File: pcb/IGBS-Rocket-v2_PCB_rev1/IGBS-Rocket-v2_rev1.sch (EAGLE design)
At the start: 220 parts, among them IC1 NCV21872DR2G, IC2 NCV21872DR2G, IC3 NCV21872DR2G, Q1 BC817, Q2 ENC-03, Q3 BSS316N-H6327, U1 STM32H750VBT6, U2 LM317BD2TG, U5 MICROSD, U6 ESP-12E/F, U8 LP324DRG4, U9 MCP6V51T-E/MS, Y1 24MHz

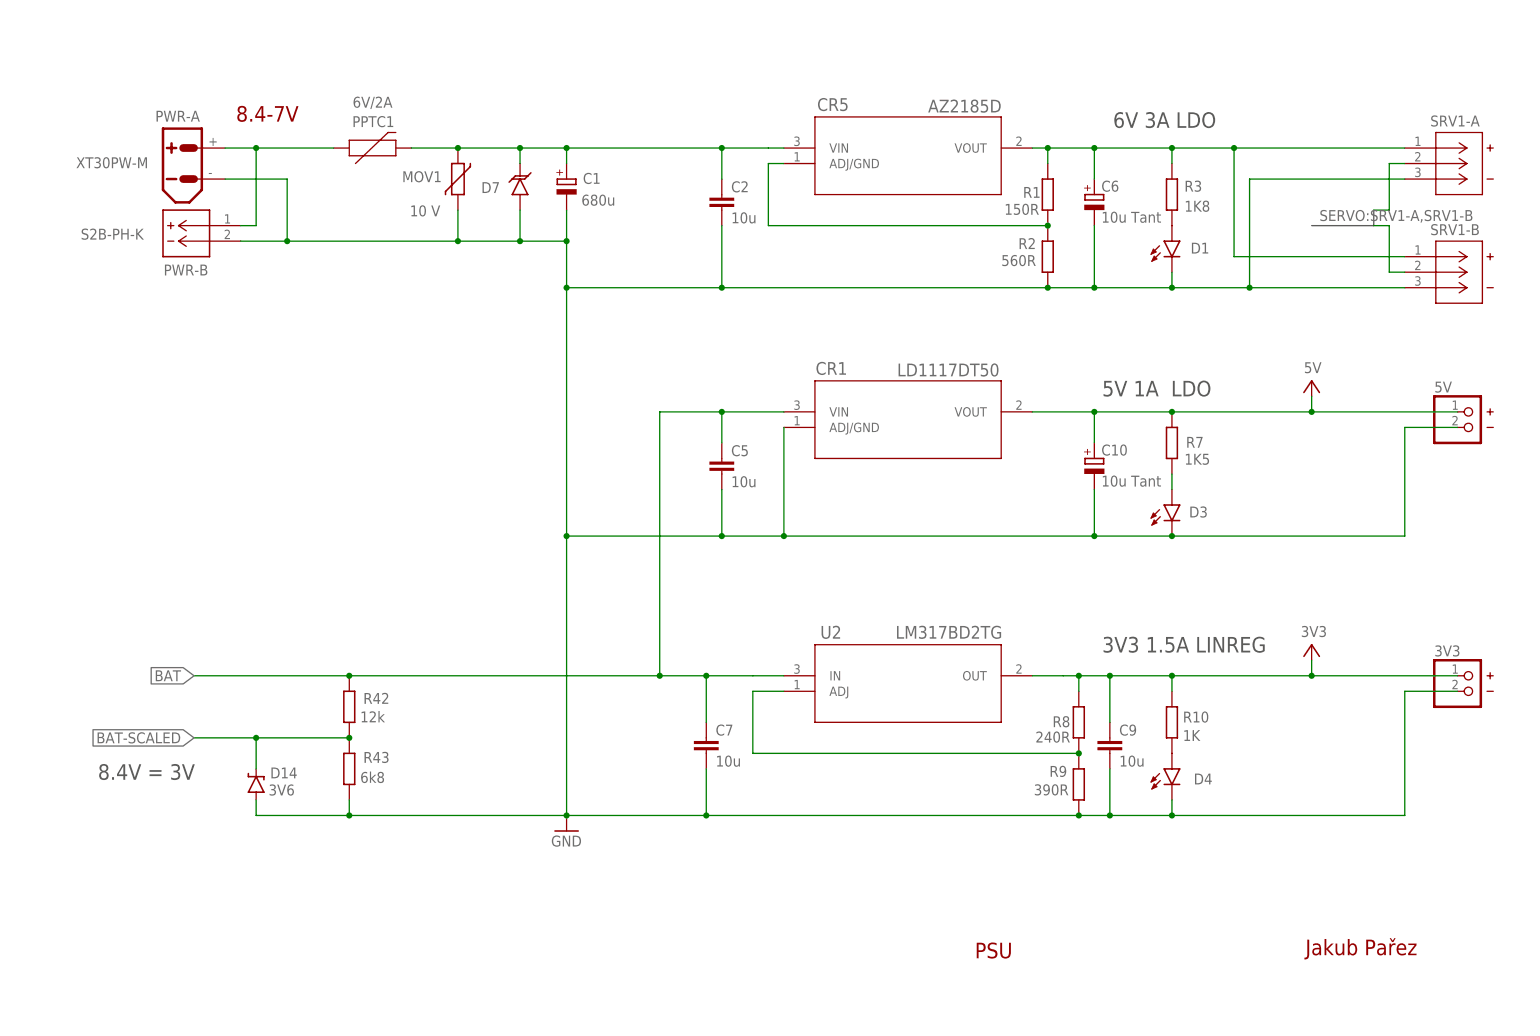
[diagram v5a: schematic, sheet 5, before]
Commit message: * PCB: 12V regulator added, P-FET HSS is now last missing part
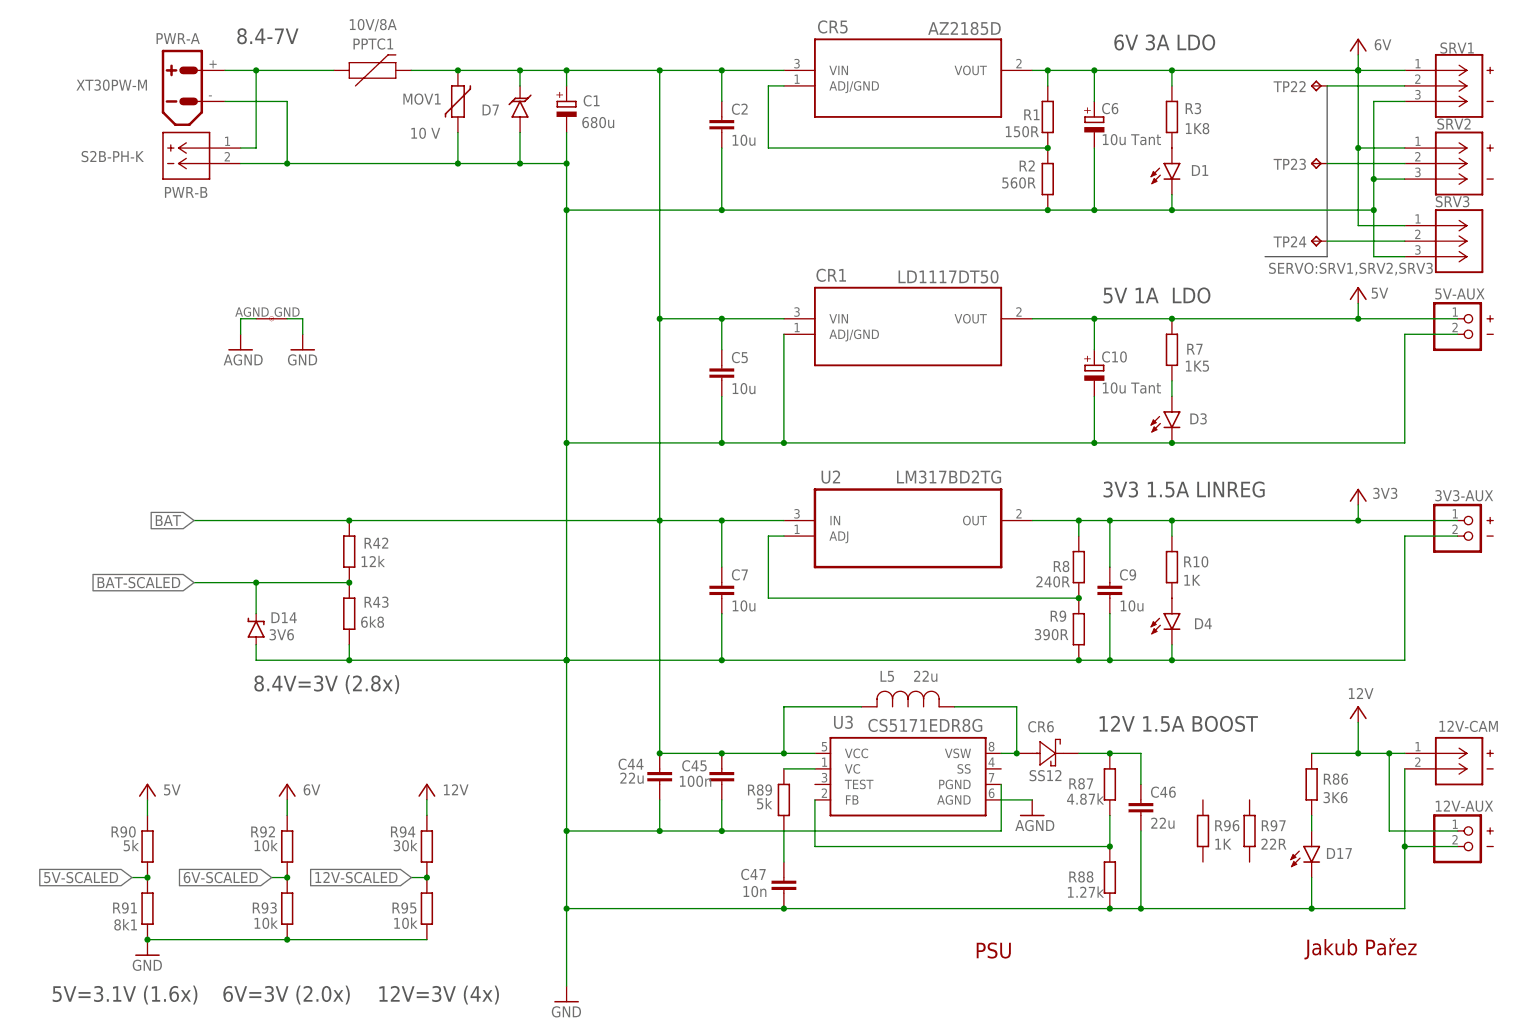
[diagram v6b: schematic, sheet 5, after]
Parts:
- removed 3V3, 5V: (no value), pinhead2:PINHD-1X2
- removed SRV1-B: S3B-XH-A(LF)(SN)CONN_S3B-XH-A(LF)(SN)_JST, jst-XH2:S3B-XH-A(LF)(SN)CONN_S3B-XH-A(LF)(SN)_JST
- added 12V-AUX, 3V3-AUX, 5V-AUX: (no value), pinhead2:PINHD-1X2
- added 12V-CAM: S2B-XH-A(LF)(SN)CONN_S2B-XH-A_JST, jst-XH2:S2B-XH-A(LF)(SN)CONN_S2B-XH-A_JST
- added C44, C46: 22u, SparkFun-Capacitors:10UF10V10%(0805)
- added C45: 100n, rcl2:C-EUC0805K
- added C47: 10n, rcl2:C-EUC0805K
- added CR6: SS12, diode2:SS12-E3/5ATDIODE_DO214AC
- added D17: GREEN, leds:LED-GREEN1206
- added L5: 22u, rcl2:744373240047IND_74437_WRE
- added R86: 3K6, rcl2:R-EU_R0603
- added R87: 4.87k, rcl2:R-EU_R0603
- added R88: 1.27k, rcl2:R-EU_R0603
- added R89, R90: 5k, rcl2:R-EU_R0603
- added R91: 8k1, rcl2:R-EU_R0603
- added R92, R93, R95: 10k, rcl2:R-EU_R0603
- added R94: 30k, rcl2:R-EU_R0603
- added R96: 1K, rcl2:R-EU_R0603
- added R97: 22R, rcl2:R-EU_R0603
- added SRV1: S3B-XH-A, jst-XH2:S3B-XH-A(LF)(SN)CONN_S3B-XH-A(LF)(SN)_JST
- added SRV3: S3B-XH-A(LF)(SN)CONN_S3B-XH-A(LF)(SN)_JST, jst-XH2:S3B-XH-A(LF)(SN)CONN_S3B-XH-A(LF)(SN)_JST
- added TP22, TP23, TP24: TPB1,27, testpad2:TPB1,27
- added U$1: SHORT, testpad2:SHORT
- added U3: CS5171EDR8G, dc-dc:CS5171EDR8GSOIC8_ONS
- GND-AUX: device pinhead2:PINHD-1X4 -> pinhead2:PINHD-1X2
- PPTC1: value 6V/2A -> 10V/8A
- SRV2: value S3B-XH-A -> S3B-XH-A(LF)(SN)CONN_S3B-XH-A(LF)(SN)_JST
- renumbered SRV1-A to SRV2
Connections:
- removed net 6V-1: C6.+, CR5.VOUT, R1.2, R3.2, SRV1-B.1, SRV2.1
- removed net SRV1-A: SRV2.2, U1A.PA0-WKUP
- removed net SRV1-B: SRV1-B.2, U1A.PA1
- new net 12V: 12V-AUX.1, 12V-CAM.1, R86.2, R94.2
- new net 12V-SCALED: R94.1, R95.2
- new net 5V-SCALED: R90.1, R91.2
- new net 6V: C6.+, CR5.VOUT, R1.2, R3.2, R92.2, SRV1.1, SRV2.1, SRV3.1
- new net 6V-SCALED: R92.1, R93.2
- new net AGND: C20.1, C25.1, C27.2, C29.1, C3.1, C30.1, C34.1, C35.1, C37.1, C38.1, C39.1, C40.1, C41.1, C42.1, C43.1, C8.1, CR2.2, CR2.3, CR3.2, CR3.3, CR4.2, CR4.3, D15.A, IC1P.V-, IC2P.V-, IC3P.V-, Q2.GND, R4.3, R6.2, R62.2, R68.3, R70.2, R71.2, R77.3, R79.2, R80.2, U$1.1, U1C.VSSA, U3.AGND, U8P.GND, U9P.GND
- new net N$27: CR6.2, L5.1, U3.VSW
- new net N$59: D17.A, R86.1
- new net N$67: C46.1, CR6.1, R87.2
- new net N$70: C47.2, R89.1
- new net N$71: R89.2, U3.VC
- new net SRV1: SRV1.2, TP22.TP, U1A.PA0-WKUP
- new net SRV2: SRV2.2, TP23.TP, U1A.PA1
- new net SRV3: SRV3.2, TP24.TP, U1A.PD14
- net 3V3: now also 3V3-AUX.1; no longer 3V3.1
- net 5V: now also 5V-AUX.1, R90.2; no longer 5V.1
- net BAT: now also C1.+, C2.1, C44.1, C45.2, CR5.VIN, D7.C, L5.2, MOV1.1, PPTC1.2, U3.VCC
- net GND: now also 12V-AUX.2, 12V-CAM.2, 3V3-AUX.2, 5V-AUX.2, C44.2, C45.1, C46.2, C47.1, D17.C, R88.1, R91.1, R93.1, R95.1, SRV1.3, SRV3.3, U$1.2, U3.PGND; no longer 3V3.2, 5V.2, C20.1, C25.1, C27.2, C29.1, C3.1, C30.1, C34.1, C35.1, C37.1, C38.1, C39.1, C40.1, C41.1, C42.1, C43.1, C8.1, CR2.2, CR2.3, CR3.2, CR3.3, CR4.2, CR4.3, D15.A, GND-AUX.3, GND-AUX.4, IC1P.V-, IC2P.V-, IC3P.V-, Q2.GND, R4.3, R6.2, R62.2, R68.3, R70.2, R71.2, R77.3, R79.2, R80.2, SRV1-B.3, U1C.VSSA, U8P.GND, U9P.GND
- net N$18: now also R87.1, R88.2, U3.FB; no longer C1.+, C2.1, CR5.VIN, D7.C, MOV1.1, PPTC1.2
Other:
- note added: "12V 1.5A BOOST"
- note added: "12V=3V (4x)"
- note added: "5V=3.1V (1.6x)"
- note added: "6V=3V (2.0x)"
- note added: "8.4V=3V (2.8x)"
- note added: "GAIN = 48 + (0 - 24.5) VOLT = 0 - 3.6V"
- note removed: "8.4V = 3V"
- moved on the sheet: C1, C10, C2, C5, C6, C7, C9, CR1, CR5, D1, D14, D3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

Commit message: + PCB schematics is DONE (added 12V BOOST + 3 servos)
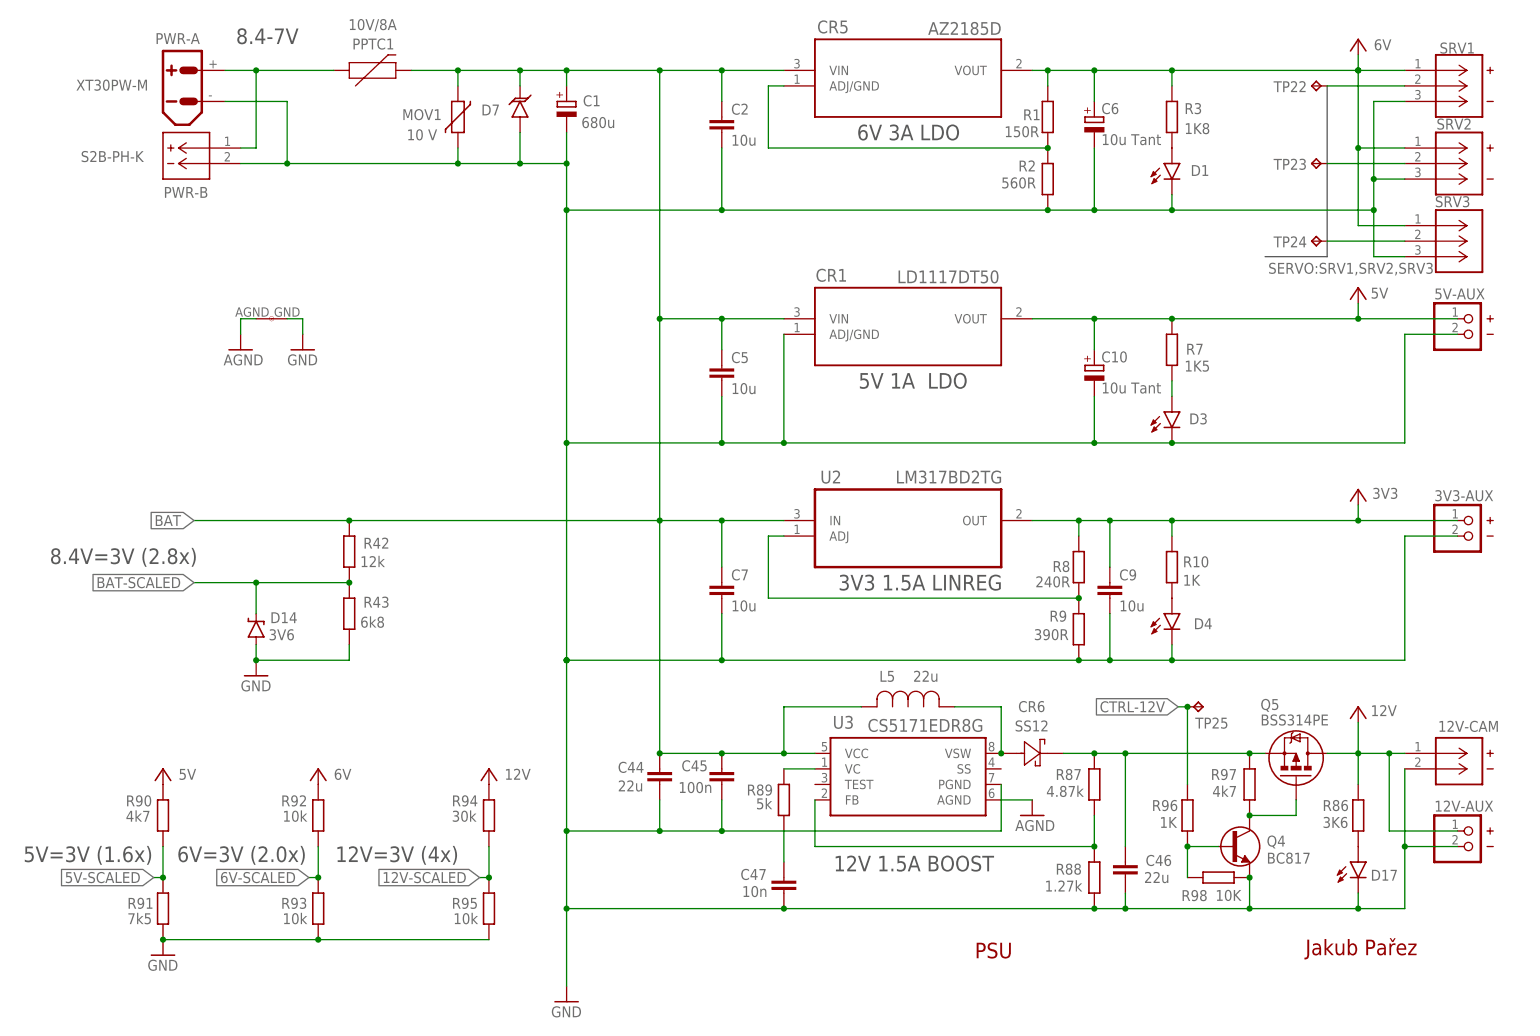
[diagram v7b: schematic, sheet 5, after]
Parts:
- added Q4: BC817, transistor-npn:BC817-16LT1SMD
- added Q5: BSS314PE, SparkFun-DiscreteSemi:MOSFET-PCHANNEL
- added R98: 10K, rcl2:R-EU_R0603
- added TP25: TPB1,27, testpad2:TPB1,27
- Q3: value BSS316N-H6327 -> BSS316N
- R90: value 5k -> 4k7; SPICEPREFIX (none) -> R
- R91: value 8k1 -> 7k5
- R97: value 22R -> 4k7
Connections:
- net N$2 renamed BAT2
- new net 12V-HOT: C46.1, CR6.1, Q5.S, R87.2, R97.1
- new net CTRL-12V: R96.2, TP25.TP, U1A.PC13
- new net N$72: Q4.C, Q5.G, R97.2
- net 12V: now also Q5.D
- net 12V-SCALED: now also U1A.PA3
- net 5V-SCALED: now also U1A.PA2
- net 6V-SCALED: now also U1A.PC1
- net ESP-RX: now also U1A.PD5; no longer U1A.PA2
- net ESP-TX: now also U1A.PD6; no longer U1A.PA3
- net GND: now also Q4.E, R98.1
- net GPS-TX: now also U1A.PA10; no longer U1A.PB15
- net ICM-MOSI: now also U1A.PB15; no longer U1A.PC1
- net N$67: now also Q4.B, R96.1, R98.2; no longer C46.1, CR6.1, R87.2
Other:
- note added: "5V=3V (1.6x)"
- note added: "F_CPU = 480 MHz (32-bit) ADC = 3.6 MSps (16-bit) FLASH = 128 KB RAM = 1 MB"
- note added: "STRAIN = 360 Ω GAIN = 48 + (0 - 24.5) VOLT = 0 - 3.6V"
- note removed: "5V=3.1V (1.6x)"
- note removed: "GAIN = 48 + (0 - 24.5) VOLT = 0 - 3.6V"
- moved on the sheet: C46, CR6, D17, MOV1, R86, R87, R88, R90, R91, R92, R93, R94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

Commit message: + PCB layout done (DXF, STEP, BRD, PNG)
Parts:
- removed 12V-AUX: (no value), pinhead2:PINHD-1X2
- B1: device modules:BMP280 -> modules:BMP280-LESSPINS
- B2: device modules:ICM-20948 -> modules:ICM-20948-LESSPINS
- H1, H2, H3, H4, H5, H6: device holes:MOUNT-PAD-ROUND2.8 -> holes3:MOUNT-PAD-ROUND2.8
- renumbered TP16 to TP26, TP17 to TP27, TP18 to TP28
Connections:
- new net 3V3-SD: C31.1, C36.1, L4.2, U5.VDD
- net 12V: no longer 12V-AUX.1
- net 3V3: no longer C31.1, C36.1, L4.2, U5.VDD
- net GND: no longer 12V-AUX.2
